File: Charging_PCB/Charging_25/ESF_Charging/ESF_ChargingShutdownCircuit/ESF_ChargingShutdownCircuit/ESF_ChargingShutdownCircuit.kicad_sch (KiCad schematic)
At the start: 40 parts, among them J1 Insulation_Monitoring_Device, J2 Conn_02x03_Counter_Clockwise, J3 Conn_02x03_Counter_Clockwise, K1 G2RL-1, K103 BMS_Relay, K104 IMD_Relay, K2 G2RL-1, Q103 Q_PMOS_GSD, Q104 Q_PMOS_GSD, Q109 Q_PMOS_GSD, Q110 Q_PMOS_GSD, Q3 NMOS, Q4 NMOS, SW2 Charger_Shutdown_Button, U10 SFH617A-1, U11 74AHC1G00, U12 SFH617A-1, U8 74LS279, U9 74AHC1G00

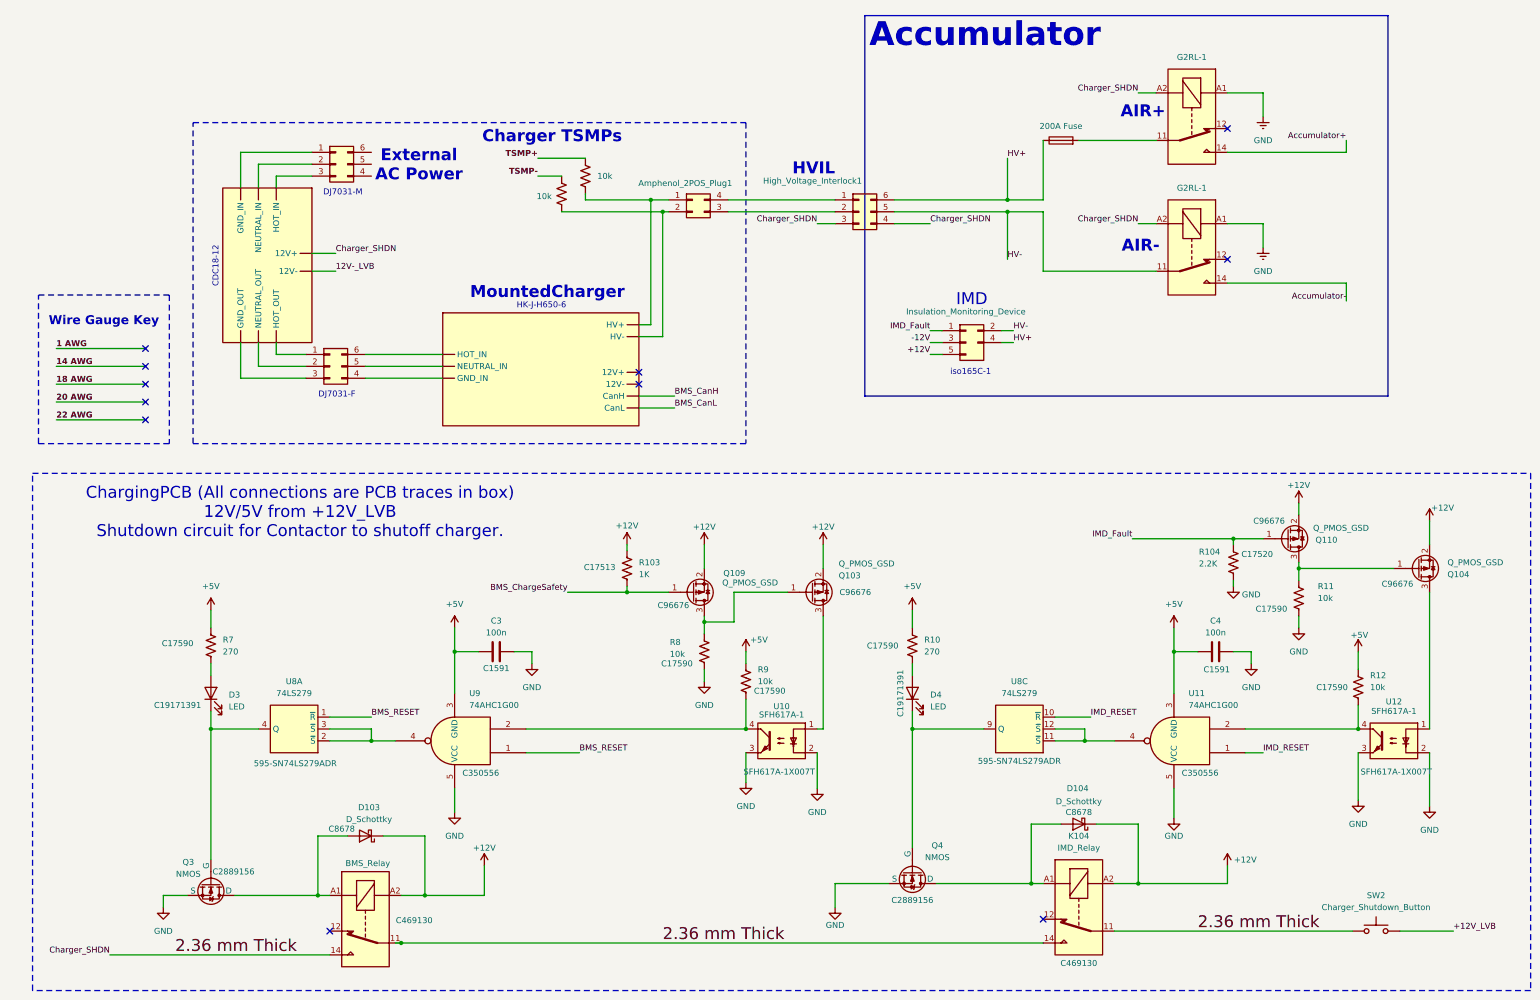
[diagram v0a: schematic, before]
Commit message: charging pcb layout
charging pcb ready to order, would like funny logo on there
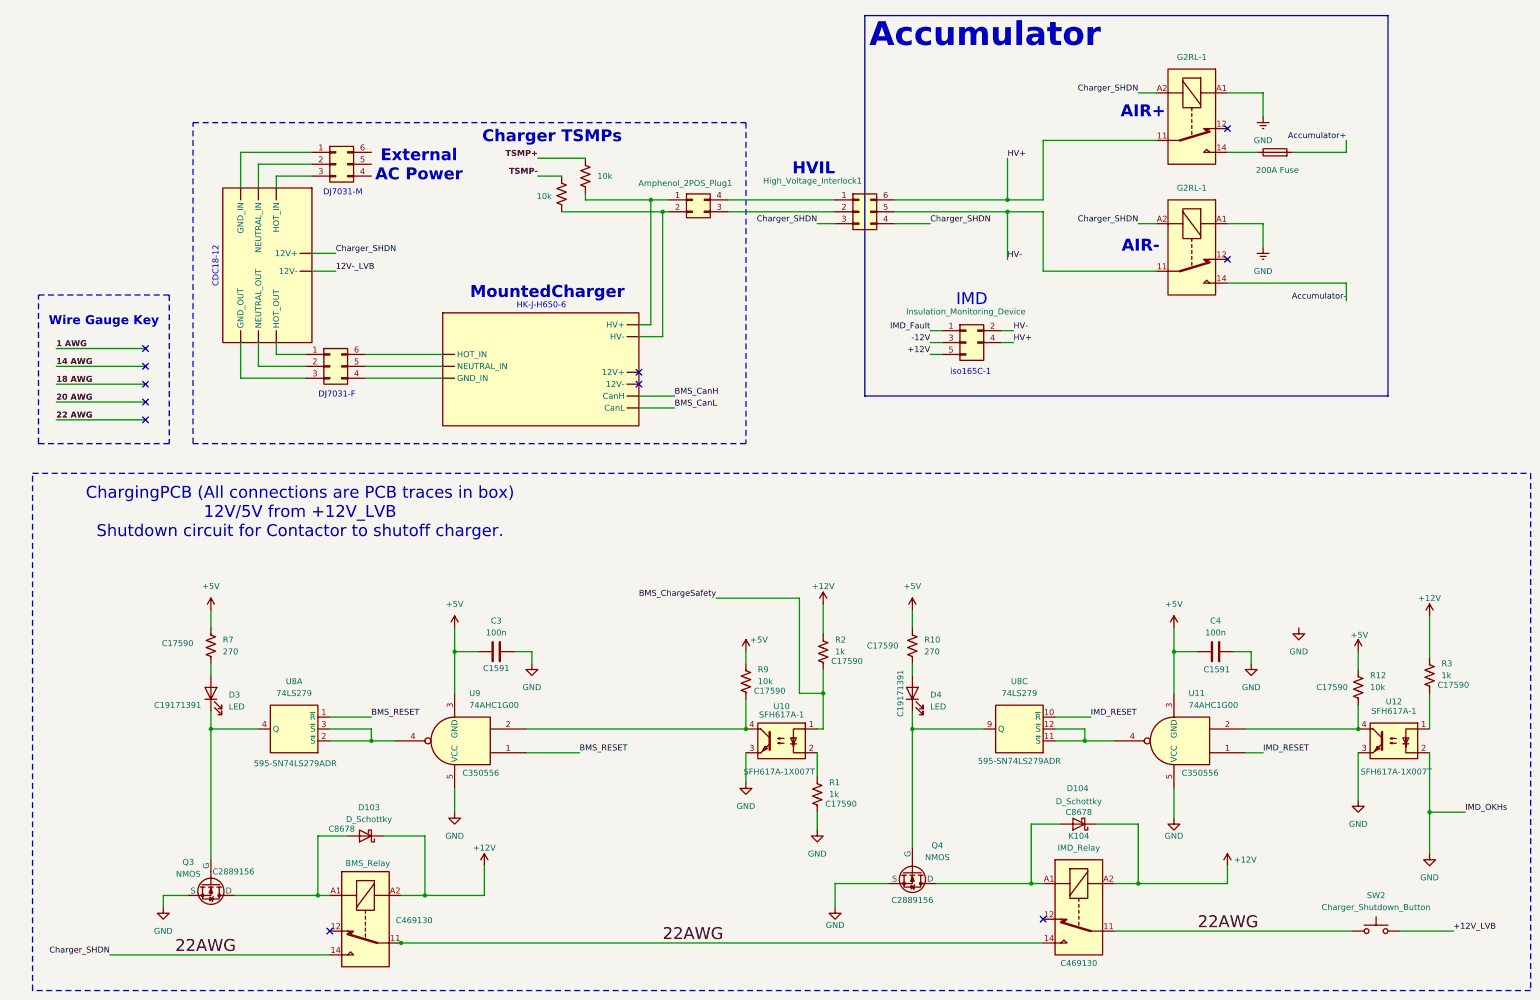
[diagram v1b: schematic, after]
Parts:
- removed F1: 200A Fuse, symbol Device:Fuse
- removed Q103, Q104, Q109, Q110: Q_PMOS_GSD, Library:SOT-523_Custom(C96676), symbol Transistor_FET:Q_PMOS_GSD
- removed R103: 1K, Resistor_SMD:R_0805_2012Metric_Pad1.20x1.40mm_HandSolder, symbol Device:R_US
- removed R104: 2.2K, Resistor_SMD:R_0805_2012Metric_Pad1.20x1.40mm_HandSolder, symbol Device:R_US
- removed R11, R8: 10k, Resistor_SMD:R_0805_2012Metric_Pad1.20x1.40mm_HandSolder, symbol Device:R_US
- added F2: 200A Fuse, symbol Device:Fuse
- added R1, R2, R3: 1k, Resistor_SMD:R_0805_2012Metric_Pad1.20x1.40mm_HandSolder, symbol Device:R_US
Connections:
- net +12V: now also R2.1, R3.1
- net Accumulator+: now also F2.2; no longer K1.14
- net BMS_ChargeSafety: now also U10.1, R2.2
- net GND: now also R1.2; no longer U10.2
- net HV+: now also K1.11
- net at U12.1: now also R3.2
- net 2.36 mm Thick renamed 22AWG
- new net: R1.1, U10.2
- new net: F2.1, K1.14

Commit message: started TS schematic
TS schematic for ESF
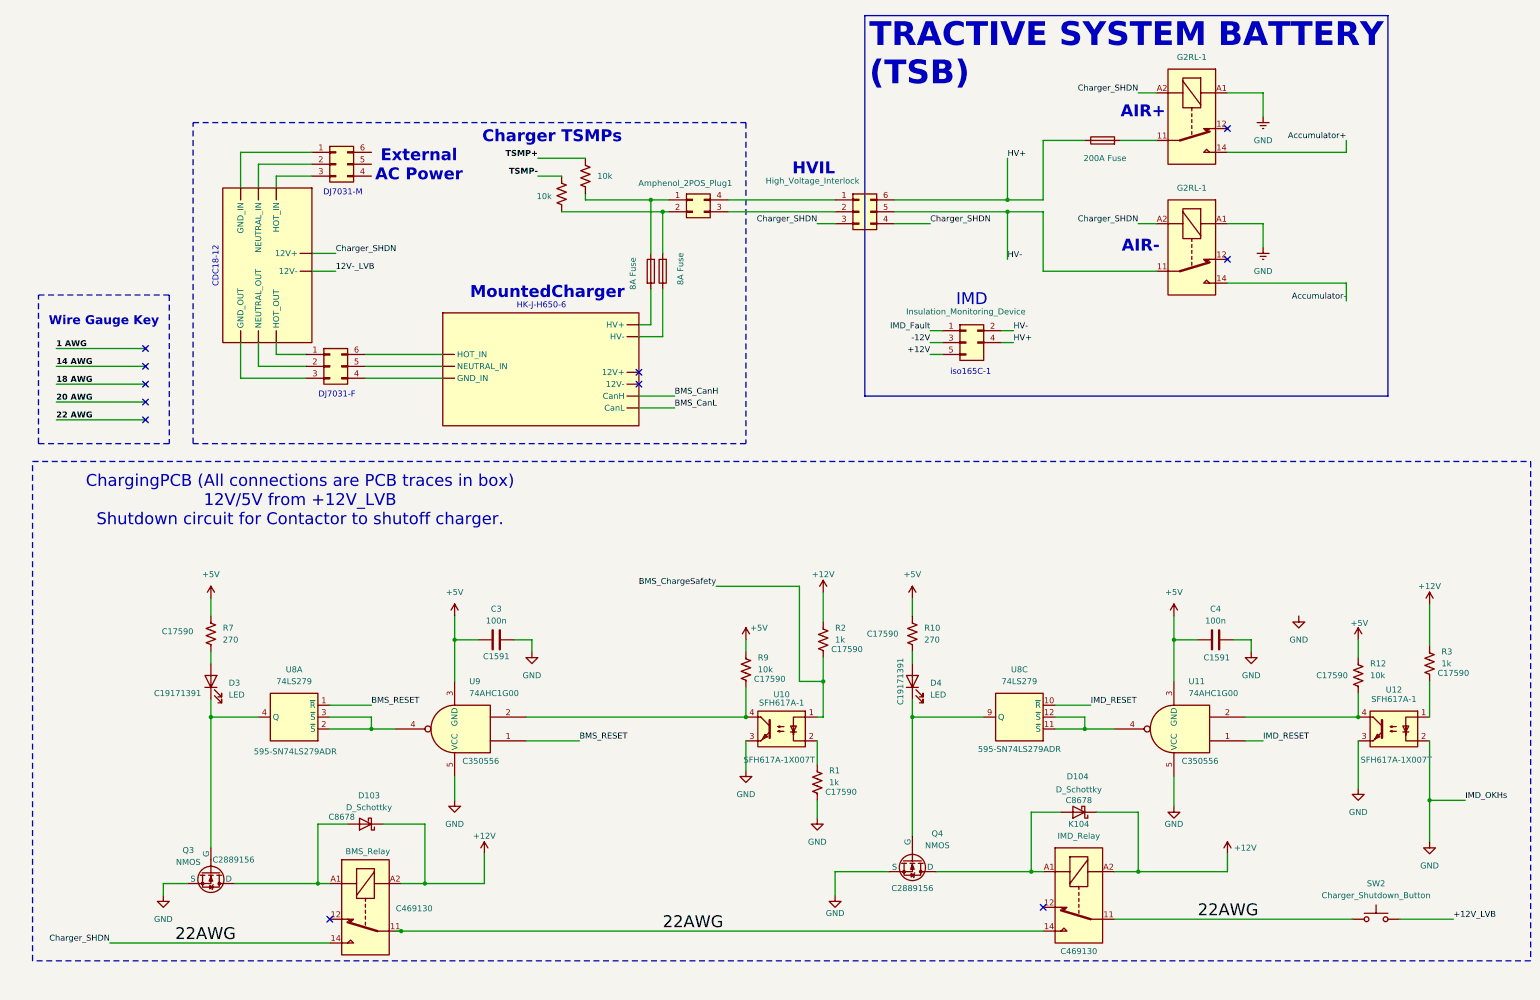
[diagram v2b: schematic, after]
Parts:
- added F1, F3: 8A Fuse, symbol Device:Fuse
- renumbered High_Voltage_Interlock1 to High_Voltage_Interlock
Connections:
- net Accumulator+: now also K1.14; no longer F2.2
- net HV+: now also F2.1; no longer K1.11
- net at 10k.2, Amphenol_2POS_Plug1.1 (Pin_1): now also F1.1; no longer U1. (CanL)
- net at 10k.2, Amphenol_2POS_Plug1.2 (Pin_2): now also F3.2; no longer U1. (CanL)
- new net: F3.1, U1. (CanL)
- new net: F1.2, U1. (CanL)
- new net: F2.2, K1.11
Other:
- moved on the sheet: C3, C4, D103, D104, D3, D4, K104, Q3, Q4, R1, R10, R12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
